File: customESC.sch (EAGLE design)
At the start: 118 parts

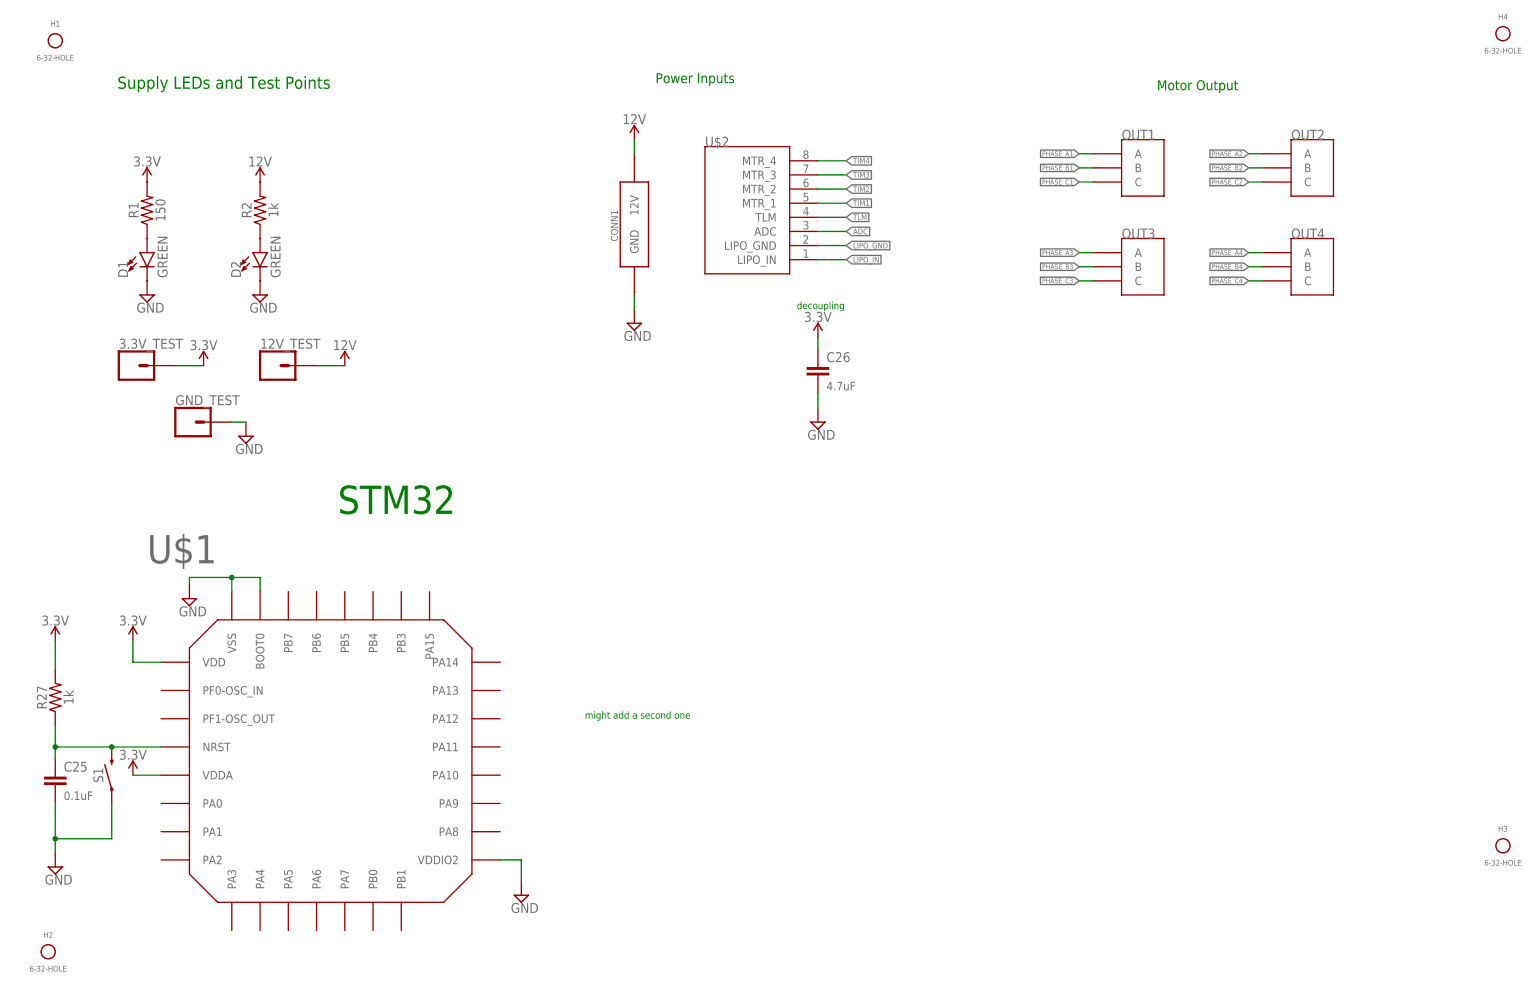
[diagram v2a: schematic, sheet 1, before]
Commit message: Finished main schematic
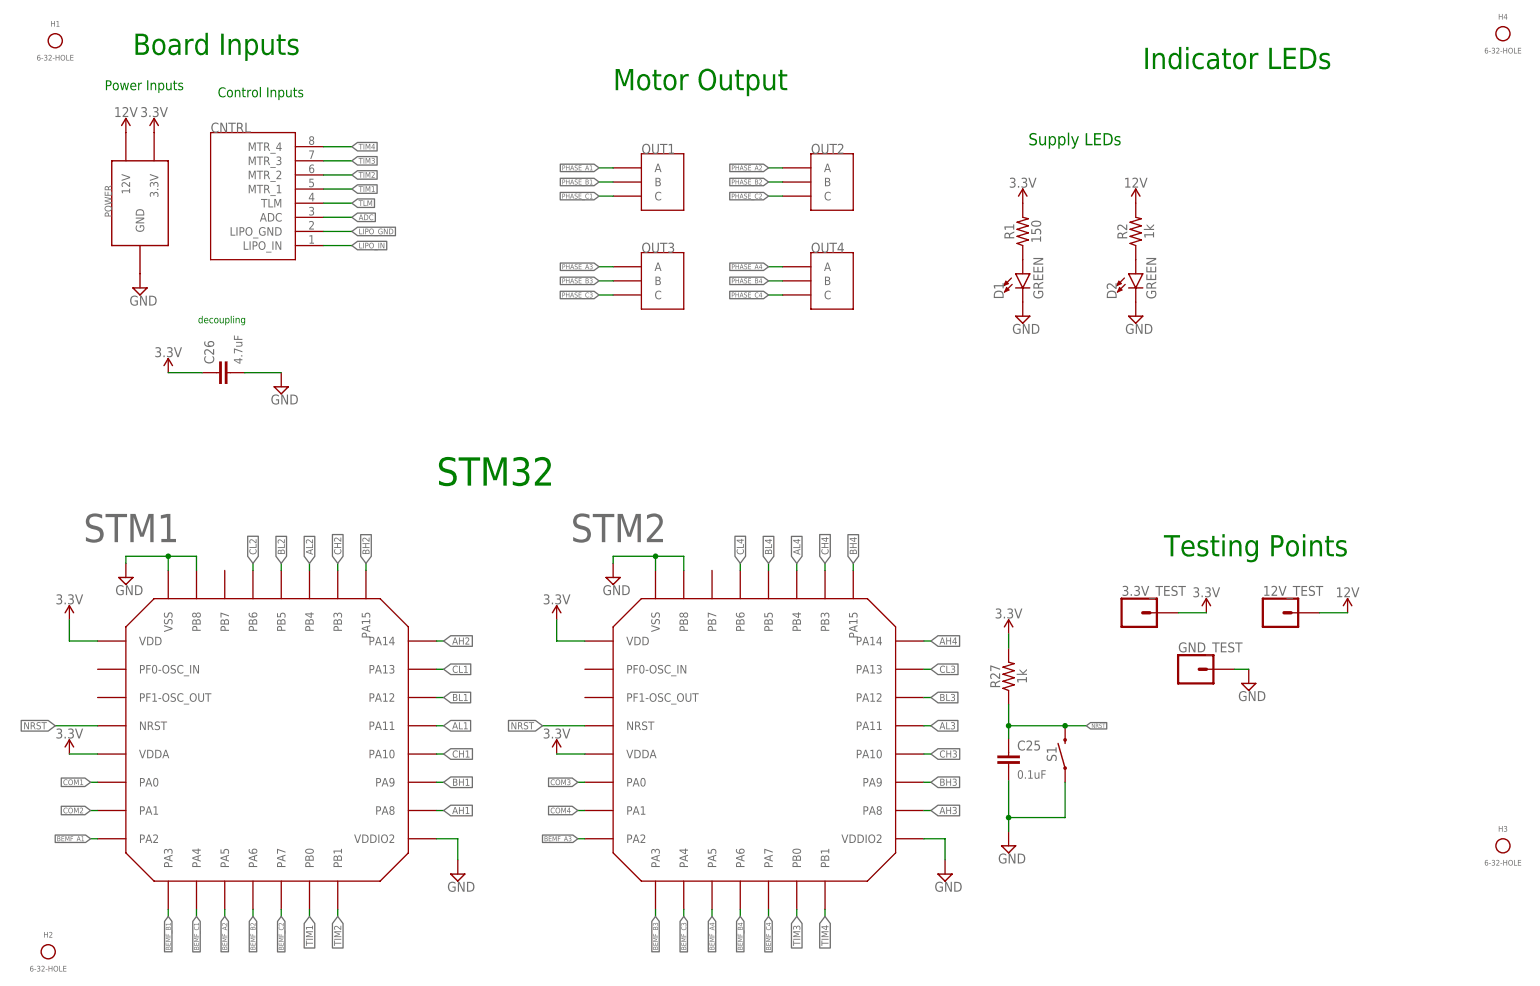
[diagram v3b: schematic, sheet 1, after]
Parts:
- removed CONN1: 12V-CONNECTOR, X15-CustomESC:12V-CONNECTOR
- removed U$1: STM32F042K6T6, X15-CustomESC:STM32F042K6T6
- removed U$2: JST_8_PIN, X15-CustomESC:JST_8_PIN
- added CNTRL: JST_8_PIN, X15-CustomESC:JST_8_PIN
- added POWER: 12V-CONNECTOR, X15-CustomESC:12V-CONNECTOR
- added R28, R29, R30, R31, R32, R33, R37, R38, R39, R40, R41, R42, R43, R44, R45, R49, R50, R51, R52, R53, R54, R55, R56, R57, R61, R62, R63, R64, R65, R66, R67, R68, R69, R73, R74, R75: 33k, SparkFun-Resistors:1KOHM-0603-1/10W-1%
- added R34, R35, R36, R46, R47, R48, R58, R59, R60, R70, R71, R72: 10k, SparkFun-Resistors:1KOHM-0603-1/10W-1%
- added STM1, STM2: STM32F042K6T6, X15-CustomESC:STM32F042K6T6
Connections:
- removed net N$63: C25.1, R27.1, S1.2, U$1.NRST
- new net BEMF_A1: R37.2, STM1.PA2
- new net BEMF_A2: R61.2, STM1.PA5
- new net BEMF_A3: R49.2, STM2.PA2
- new net BEMF_A4: R73.2, STM2.PA5
- new net BEMF_B1: R38.2, STM1.PA3
- new net BEMF_B2: R62.2, STM1.PA6
- new net BEMF_B3: R50.2, STM2.PA3
- new net BEMF_B4: R74.2, STM2.PA6
- new net BEMF_C1: R39.2, STM1.PA4
- new net BEMF_C2: R63.2, STM1.PA7
- new net BEMF_C3: R51.2, STM2.PA4
- new net BEMF_C4: R75.2, STM2.PA7
- new net COM1: R28.1, R29.1, R30.1, STM1.PA0
- new net COM2: R52.1, R53.1, R54.1, STM1.PA1
- new net COM3: R40.1, R41.1, R42.1, STM2.PA0
- new net COM4: R64.1, R65.1, R66.1, STM2.PA1
- new net N$64: R28.2, R31.1, R34.2, R37.1
- new net N$65: R29.2, R32.1, R35.2, R38.1
- new net N$66: R30.2, R33.1, R36.2, R39.1
- new net N$67: R40.2, R43.1, R46.2, R49.1
- new net N$68: R41.2, R44.1, R47.2, R50.1
- new net N$69: R42.2, R45.1, R48.2, R51.1
- new net N$70: R52.2, R55.1, R58.2, R61.1
- new net N$71: R53.2, R56.1, R59.2, R62.1
- new net N$72: R54.2, R57.1, R60.2, R63.1
- new net N$73: R64.2, R67.1, R70.2, R73.1
- new net N$74: R65.2, R68.1, R71.2, R74.1
- new net N$75: R66.2, R69.1, R72.2, R75.1
- new net NRST: C25.1, R27.1, S1.2, STM1.NRST, STM2.NRST
- net ADC: now also CNTRL.ADC; no longer U$2.ADC
- net AH1: now also STM1.PA8
- net AH2: now also STM1.PA14
- net AH3: now also STM2.PA8
- net AH4: now also STM2.PA14
- net AL1: now also STM1.PA11
- net AL2: now also STM1.PB4
- net AL3: now also STM2.PA11
- net AL4: now also STM2.PB4
- net BH1: now also STM1.PA9
- net BH2: now also STM1.PA15
- net BH3: now also STM2.PA9
- net BH4: now also STM2.PA15
- net BL1: now also STM1.PA12
- net BL2: now also STM1.PB5
- net BL3: now also STM2.PA12
- net BL4: now also STM2.PB5
- net CH1: now also STM1.PA10
- net CH2: now also STM1.PB3
- net CH3: now also STM2.PA10
- net CH4: now also STM2.PB3
- net CL1: now also STM1.PA13
- net CL2: now also STM1.PB6
- net CL3: now also STM2.PA13
- net CL4: now also STM2.PB6
- net GND: now also POWER.GND, R34.1, R35.1, R36.1, R46.1, R47.1, R48.1, R58.1, R59.1, R60.1, R70.1, R71.1, R72.1, STM1.PB8, STM1.VDDIO2, STM1.VSS, STM2.PB8, STM2.VDDIO2, STM2.VSS; no longer CONN1.GND, U$1.BOOT0, U$1.VDDIO2, U$1.VSS
- net LIPO_GND: now also CNTRL.LIPO_GND; no longer U$2.LIPO_GND
- net LIPO_IN: now also CNTRL.LIPO_IN; no longer U$2.LIPO_IN
- net PHASE_A1: now also R31.2
- net PHASE_A2: now also R55.2
- net PHASE_A3: now also R43.2
- net PHASE_A4: now also R67.2
- net PHASE_B1: now also R32.2
- net PHASE_B2: now also R56.2
- net PHASE_B3: now also R44.2
- net PHASE_B4: now also R68.2
- net PHASE_C1: now also R33.2
- net PHASE_C2: now also R57.2
- net PHASE_C3: now also R45.2
- net PHASE_C4: now also R69.2
- net TIM1: now also CNTRL.MTR_1, STM1.PB0; no longer U$2.MTR_1
- net TIM2: now also CNTRL.MTR_2, STM1.PB1; no longer U$2.MTR_2
- net TIM3: now also CNTRL.MTR_3, STM2.PB0; no longer U$2.MTR_3
- net TIM4: now also CNTRL.MTR_4, STM2.PB1; no longer U$2.MTR_4
- net TLM: now also CNTRL.TLM; no longer U$2.TLM
- net VCC_1: now also POWER.3.3V, STM1.VDD, STM1.VDDA, STM2.VDD, STM2.VDDA; no longer U$1.VDD, U$1.VDDA
- net VCC_2: now also POWER.12V; no longer CONN1.12V
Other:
- note added: "Back EMF Detection"
- note added: "Board Inputs"
- note added: "Control Inputs"
- note added: "Indicator LEDs"
- note added: "Supply LEDs"
- note added: "Testing Points"
- note removed: "Supply LEDs and Test Points"
- note removed: "might add a second one"
- moved on the sheet: 12V_TEST, 3.3V_TEST, C25, C26, D1, D2, GND_TEST, OUT1, OUT2, OUT3, OUT4, R1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
